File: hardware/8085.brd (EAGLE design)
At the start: 167.9 x 122.5 mm, 53 parts, among them IC10 74HCT00N, IC11 74HCT245DW, IC2 74AC573N, IC3 ATF16V8BP3, IC4 74AC00D, IC5 74HCT245DW, IC6 74AC273N, IC7 74HCT139N, IC8 7404N, IC9 74HCT138N

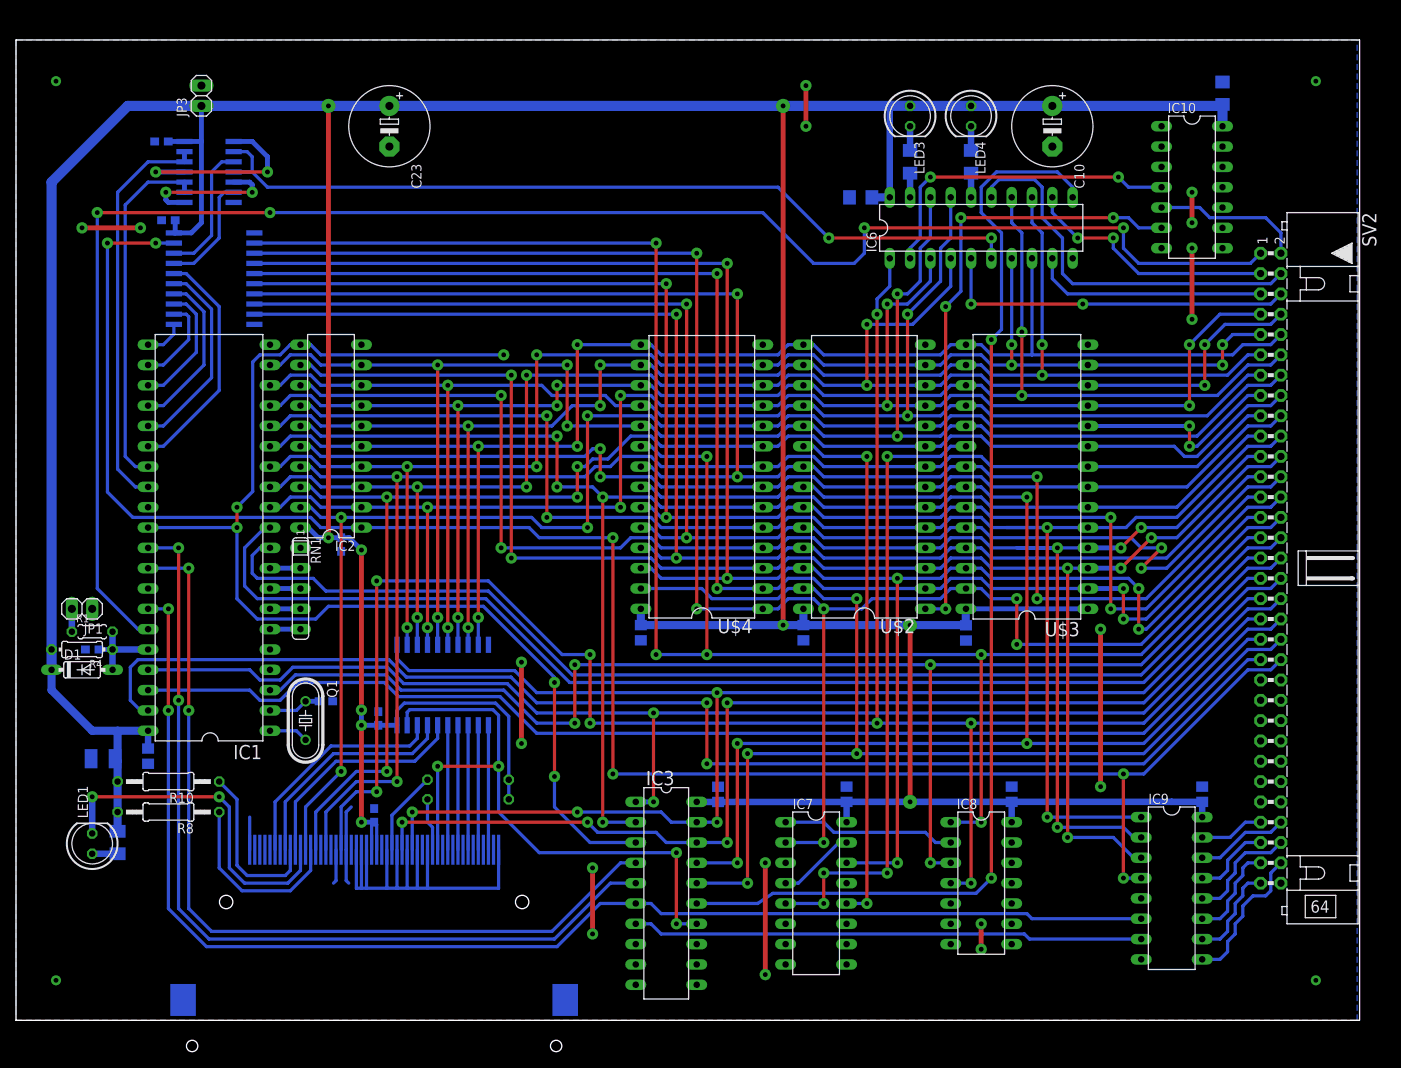
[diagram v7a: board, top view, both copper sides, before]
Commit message: Bugs in PCB board fixed
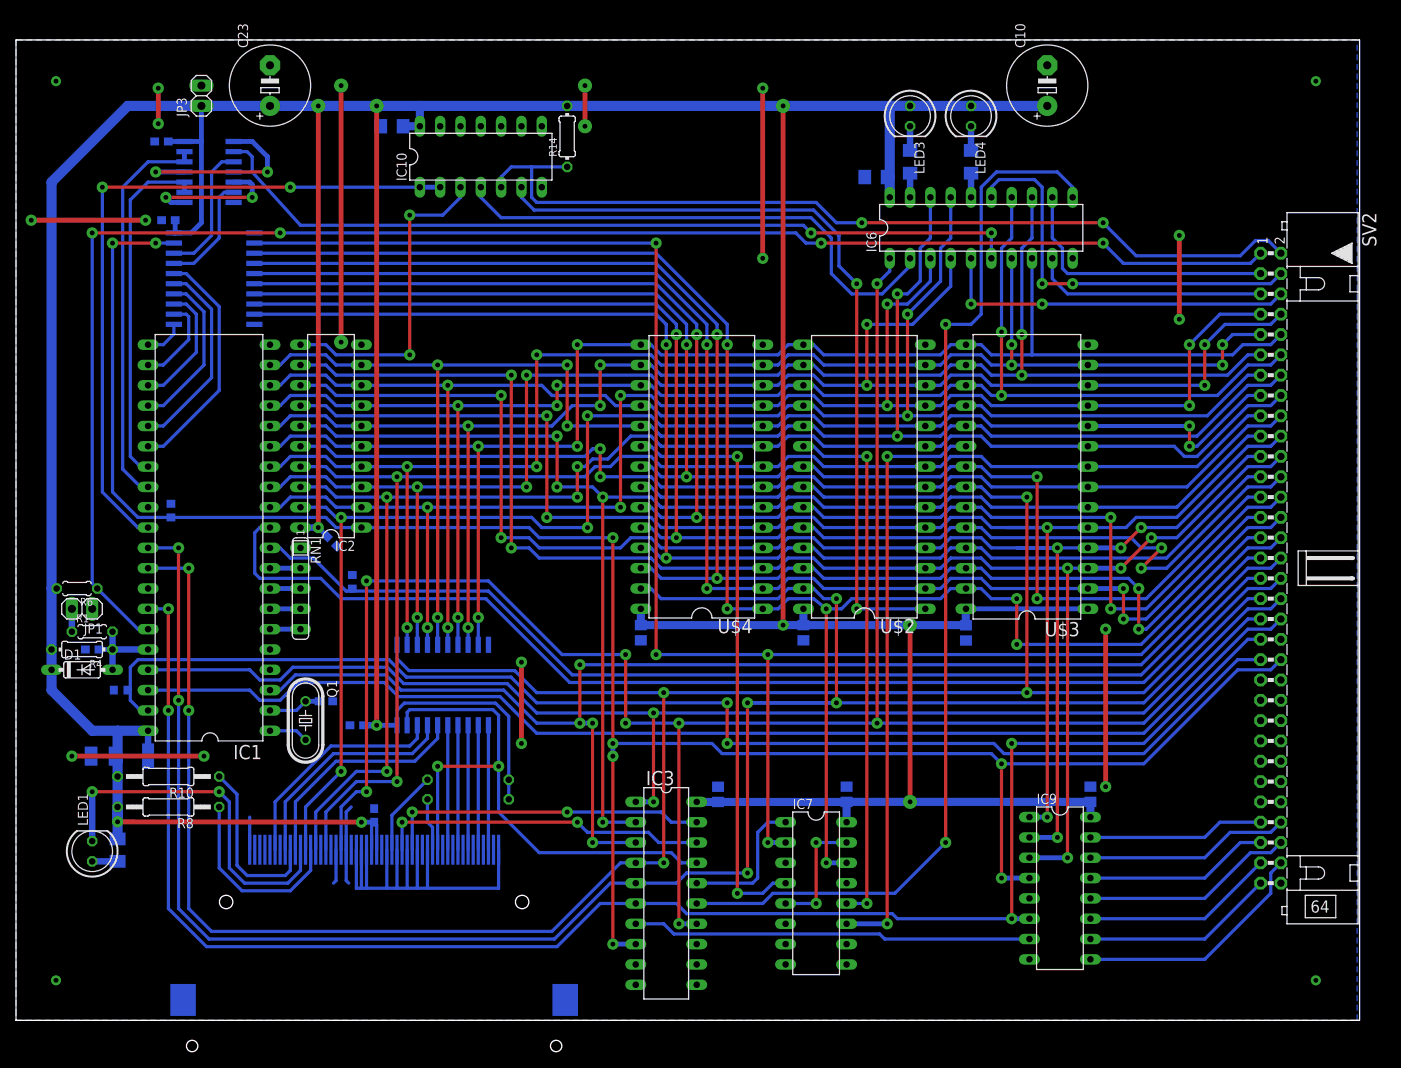
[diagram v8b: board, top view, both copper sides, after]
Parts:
- removed C12: 100n, rcl:C0805
- removed IC8: 7404N, 74xx-us:DIL14
- added R12, R13, R9: (no value), rcl:R0603
- added R14: (no value), rcl:0204/7
- added R6: (no value), rcl:0204/5
- IC2: value 74AC573N -> 74HCT574N
- moved C15 103.9 mm to (47.0, 111.8), turned to 0 degrees
- moved IC10 89.0 mm to (58.1, 108.0), turned to 0 degrees
- moved C23 15.8 mm to (31.8, 116.8), turned to 90 degrees
- moved C13 14.0 mm to (134.3, 28.3)
- moved IC9 14.0 mm to (130.5, 16.5)
- moved C10 5.12 mm to (128.9, 116.8), turned to 90 degrees
- moved C9 3.17 mm to (107.5, 105.4)
- moved C5 2.82 mm to (42.6, 36.9), turned to 0 degrees
- moved C21 1.21 mm to (39.5, 59.9), turned to 225 degrees
- moved LED1 0.95 mm to (9.53, 21.1)
- moved R5 0.95 mm to (12.7, 21.3)
- moved R10 0.64 mm to (19.1, 30.5)
- moved R8 0.64 mm to (19.1, 26.7)
- moved C16 0.32 mm to (10.9, 33.0)
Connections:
- removed net !A15: IC7.1, IC8.2
- removed net IO_RD: CON1.34, IC11.1, IC3.19, SV2.34
- removed net IO_WR: CON1.35, IC3.18, SV2.35
- removed net MEM_RD: IC3.17, SV2.39, U$2.22, U$3.22, U$4.22
- removed net MEM_WR: IC3.16, SV2.40, U$2.27, U$4.27
- new net !ALE: IC10.3, IC2.11
- new net CF_DELAYED_RD: CON1.34, IC3.19
- new net CF_DELAYED_WR: CON1.35, IC3.18
- new net CS_RAM1: IC7.4, U$4.20
- new net MEM_EN: IC3.16, IC7.1
- net !RESET: now also IC3.14; no longer IC8.4
- net 8275_DACK: now also R14.1
- net A13: no longer IC7.14
- net A14: now also IC7.14; no longer IC7.2
- net A15: now also IC7.2; no longer IC8.1, U$4.20
- net AEN: now also IC3.8, R9.1
- net ALE: now also IC10.1, IC10.2; no longer IC2.11, IC3.3
- net CF_CS0: now also IC3.17; no longer IC3.14
- net CS_EPROM: now also IC7.11; no longer IC7.5
- net GND: now also R12.1, R13.1, R9.2, SV2.40; no longer C12.2, IC10.1, IC10.2, IC3.8, IC8.11, IC8.13, IC8.5, IC8.7, IC8.9
- net HRQ: now also R12.2
- net INT: now also R13.2
- net IO_M: now also SV2.39
- net N$19: now also IC7.5; no longer IC7.4
- net RD: now also IC11.1, SV2.34, U$2.22, U$3.22, U$4.22
- net RDYIN: now also R6.1
- net RESET: now also IC3.3; no longer IC8.3
- net VCC: now also R14.2, R6.2; no longer C12.1, IC8.14
- net WR: now also SV2.35, U$2.27, U$4.27
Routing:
- net RD: track 108.2 -> 328.2 mm, vias 2 -> 6
- net IO_RD: track 179.4 -> 0.00 mm, vias 4 -> 0
- net MEM_RD: track 172.5 -> 0.00 mm, vias 4 -> 0
- net WR: track 110.5 -> 266.6 mm, vias 2 -> 6
- net MEM_WR: track 143.7 -> 0.00 mm, vias 4 -> 0
- net IO_WR: track 134.7 -> 0.00 mm, vias 4 -> 0
- net 8275_DACK: track 18.8 -> 112.0 mm, vias 0 -> 2
- net CS_RAM1: track 0.00 -> 73.8 mm, vias 0 -> 2
- net ALE: track 147.6 -> 87.9 mm, vias 5 -> 2
- net GND: track 159.7 -> 213.4 mm
- net A13: track 234.4 -> 186.8 mm, vias 6 -> 4
- net IO_M: track 166.6 -> 211.0 mm, vias 2 -> 4
- net CF_DELAYED_WR: track 0.00 -> 41.3 mm, vias 0 -> 2
- net CF_DELAYED_RD: track 0.00 -> 40.8 mm, vias 0 -> 2
- net !ALE: track 0.00 -> 40.2 mm, vias 0 -> 2
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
